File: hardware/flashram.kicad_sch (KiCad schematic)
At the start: 2 parts, among them U2 MT25QL256ABA1EW7-0SIT, U3 MT41K256M16TW-107:P

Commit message: last commit for a while, i have to change the fpga and i dont have the time, money, or motivation to do that
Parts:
- added C75: 4.7u, symbol Device:C
- added C76, C77, C78, C79, C80, C81, C85: 0.1u, symbol Device:C
- added C82, C84, C86, C87, C88: 10u, symbol Device:C
- added C83: 1000p, symbol Device:C
- added R11: 240, symbol Device:R
- added R12, R13, R14, R15, R16: 10k, symbol Device:R
- added U9: TPS51200DRCR, DRC0010J, symbol arcticvideo:TPS51200DRCR
- renumbered U2 to U7, U3 to U8
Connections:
- net GND: now reaches U8.97 (EPAD)
- net GND: now also U7.4 (VSS), U7.9 (GND), U8.A9 (VSS), U8.B1 (VSSQ), U8.B3 (VSS), U8.B9 (VSSQ), U8.D1 (VSSQ), U8.D8 (VSSQ), U8.E1 (VSS), U8.E2 (VSSQ), U8.E8 (VSSQ), U8.F9 (VSSQ), U8.G1 (VSSQ), U8.G8 (VSS), U8.G9 (VSSQ), U8.J2 (VSS), U8.J8 (VSS), U8.M1 (VSS), U8.M9 (VSS), U8.P1 (VSS), U8.P9 (VSS), U8.T1 (VSS), U8.T9 (VSS), C75.1, C76.1, C77.1, C78.1, C79.1, C80.1, C81.1, C82.1, C83.1, C84.1, C85.1, C86.1, C87.1, C88.1, R11.1, R16.1, U9.11 (PAD), U9.4 (PGND), U9.8 (GND)
- net +1V35: now reaches U8.A1 (VDDQ)
- net +1V35: now also U8.A8 (VDDQ), U8.B2 (VDD), U8.C1 (VDDQ), U8.C9 (VDDQ), U8.D2 (VDDQ), U8.D9 (VDD), U8.E9 (VDDQ), U8.F1 (VDDQ), U8.G7 (VDD), U8.H2 (VDDQ), U8.H9 (VDDQ), U8.K2 (VDD), U8.K8 (VDD), U8.N1 (VDD), U8.N9 (VDD), U8.R1 (VDD), U8.R9 (VDD), C75.2, C76.2, C77.2, C78.2, C80.2, C82.2, C84.2, R15.2, U9.2 (VLDOIN)
- net DQ13: now reaches U8.A2 (DQ13)
- net DQ15: now reaches U8.A3 (DQ15)
- net DQ12: now reaches U8.A7 (DQ12)
- net *UDQS: now reaches U8.B7 (*UDQS)
- net DQ14: now reaches U8.B8 (DQ14)
- net DQ11: now reaches U8.C2 (DQ11)
- net DQ9: now reaches U8.C3 (DQ9)
- net UDQS: now reaches U8.C7 (UDQS)
- net DQ10: now reaches U8.C8 (DQ10)
- net UDM: now reaches U8.D3 (UDM)
- net DQ8: now reaches U8.D7 (DQ8)
- net DQ0: now reaches U8.E3 (DQ0)
- net LDM: now reaches U8.E7 (LDM)
- net DQ2: now reaches U8.F2 (DQ2)
- net LDQS: now reaches U8.F3 (LDQS)
- net DQ1: now reaches U8.F7 (DQ1)
- net DQ3: now reaches U8.F8 (DQ3)
- net DQ6: now reaches U8.G2 (DQ6)
- net *LDQS: now reaches U8.G3 (*LDQS)
- net +0V675: now reaches U8.H1 (VREFDQ)
- net +0V675: now also U8.M8 (VREFCA), C79.2, C81.2, C86.2, C87.2, C88.2, U9.3 (VO), U9.5 (VOSNS)
- net DQ4: now reaches U8.H3 (DQ4)
- net DQ7: now reaches U8.H7 (DQ7)
- net DQ5: now reaches U8.H8 (DQ5)
- net *RAS: now reaches U8.J3 (*RAS)
- net CK: now reaches U8.J7 (CK)
- net ODT: now reaches U8.K1 (ODT)
- net *CAS: now reaches U8.K3 (*CAS)
- net *CK: now reaches U8.K7 (*CK)
- net CKE: now reaches U8.K9 (CKE)
- net *CS: now reaches U8.L2 (*CS)
- net *WE: now reaches U8.L3 (*WE)
- net A10/AP: now reaches U8.L7 (A10/AP)
- net ZQ: now reaches U8.L8 (ZQ)
- net ZQ: now also R11.2
- net BA0: now reaches U8.M2 (BA0)
- net BA2: now reaches U8.M3 (BA2)
- net A3: now reaches U8.N2 (A3)
- net A0: now reaches U8.N3 (A0)
- net A12/*BC: now reaches U8.N7 (A12/*BC)
- net BA1: now reaches U8.N8 (BA1)
- net A5: now reaches U8.P2 (A5)
- net A2: now reaches U8.P3 (A2)
- net A1: now reaches U8.P7 (A1)
- net A4: now reaches U8.P8 (A4)
- net A7: now reaches U8.R2 (A7)
- net A9: now reaches U8.R3 (A9)
- net A11: now reaches U8.R7 (A11)
- net A6: now reaches U8.R8 (A6)
- net *RESET: now reaches U8.T2 (*RESET)
- net A13: now reaches U8.T3 (A13)
- net A14: now reaches U8.T7 (A14)
- net A8: now reaches U8.T8 (A8)
- net CS#: now reaches U7.1 (S#)
- net CS#: now also R13.1
- net SPI_MISO: now reaches U7.2 (DQ1)
- net WP#: now reaches U7.3 (W#/DQ2)
- net WP#: now also R12.1
- net SPI_MOSI: now reaches U7.5 (DQ0)
- net CCLK_0: now reaches U7.6 (C)
- net HOLD#: now reaches U7.7 (DQ3/HOLD#)
- net HOLD#: now also R14.1
- net +3V3: now reaches U7.8 (VCC)
- net +3V3: now also R12.2, R13.2, R14.2
- new net: C83.2, R15.1, R16.2, U9.1 (REFIN)
- new net VTTREF: C85.2, U9.6 (REFOUT)
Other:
- moved on the sheet: U7, U8

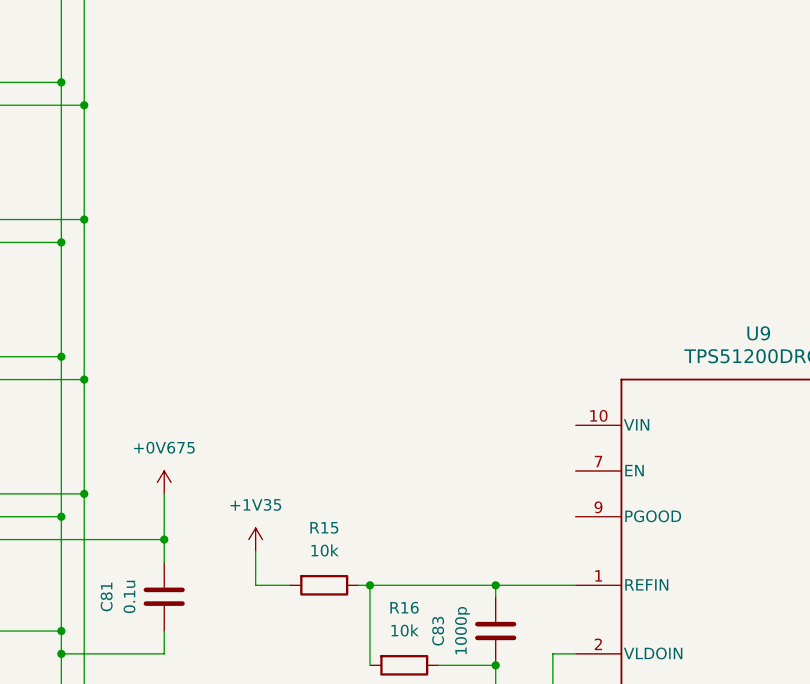
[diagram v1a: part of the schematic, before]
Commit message: finished schematic!!! :D (before peer review)
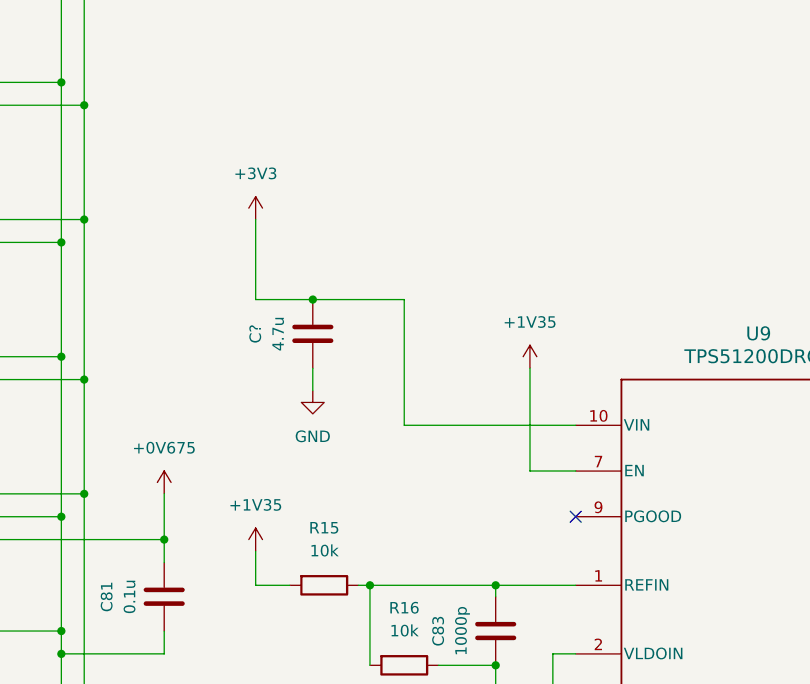
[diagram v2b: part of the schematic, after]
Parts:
- added C?: 4.7u, symbol Device:C
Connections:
- net +1V35: now also U9.7 (EN)
- net +3V3: now also U9.10 (VIN), C?.2
- net GND: now also C?.1
- no-connect marks 0 -> 1

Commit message: readable changes
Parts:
- gave numbers to parts that had none: 1
- renumbered C78 to C100, C79 to C101, C80 to C102, C81 to C103, C82 to C105, C83 to C106, C84 to C107, C85 to C108, C86 to C109, C87 to C110, C88 to C111, C75 to C97, C76 to C98, C77 to C99, R11 to R35, R12 to R36, R13 to R37, R14 to R38, R15 to R39, R16 to R40, U9 to U10, U7 to U8, U8 to U9
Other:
- moved on the sheet: C104, C109, C110, C111

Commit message: pcb routing
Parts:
- C100, C101, C102, C103, C104, C105, C106, C107, C108, C109, C110, C111, C97, C98, C99: footprint (none) -> Capacitor_SMD:C_0402_1005Metric
- R33: renamed from R35; footprint (none) -> Resistor_SMD:R_0402_1005Metric
- R34: renamed from R36; footprint (none) -> Resistor_SMD:R_0402_1005Metric
- R35: renamed from R37; footprint (none) -> Resistor_SMD:R_0402_1005Metric
- R36: renamed from R38; footprint (none) -> Resistor_SMD:R_0402_1005Metric
- R37: renamed from R39; footprint (none) -> Resistor_SMD:R_0402_1005Metric
- R38: renamed from R40; footprint (none) -> Resistor_SMD:R_0402_1005Metric
- U10: footprint DRC0010J -> arcticvideo:DRC0010J
- U8: footprint SON_EW7-0SIT_MRN -> arcticvideo:SON_EW7-0SIT_MRN
- U9: footprint FBGA96_8X14_MRN -> arcticvideo:FBGA96_8X14_MRN
